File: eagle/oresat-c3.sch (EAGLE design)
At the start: 161 parts, among them J1 J-SAMTEC-TFM-110-X1-XXX-D-RA, J10 U.FL, J11 U.FL, J13 U.FL, J14 U.FL, J15 HARWIN-2X8X1.27, J19 HARWIN-2X8X1.27, J2 U.FL, J3 U.FL, J4 U.FL, J5 2-1734592-0, J6 J-SAMTEC-TFM-120-X1-XXX-D-RA, J8 U.FL, J9 U.FL, Q1 MOSFET-PCH-SOT23-6, U1 MAX892LEUA+T21-0036K-L, U11 U-ONSEMI-AX5043, U12 LP2985XX-N, U13 U-ONSEMI-AX5043, U14 LP2985XX-N, U2 TCAN330, U3 TCAN330, U4 TPS259621 - eFuse, U5 TPS62111RSA, U7 STM32F446RE, U8 UT01VS33DFLATDI_8, U9 SFEM016GB1EM1TO-A-HG-111-STD, X1 16MHZ-2.5x2mm, X3 TAITIEN-TY, X4 TAITIEN-TY

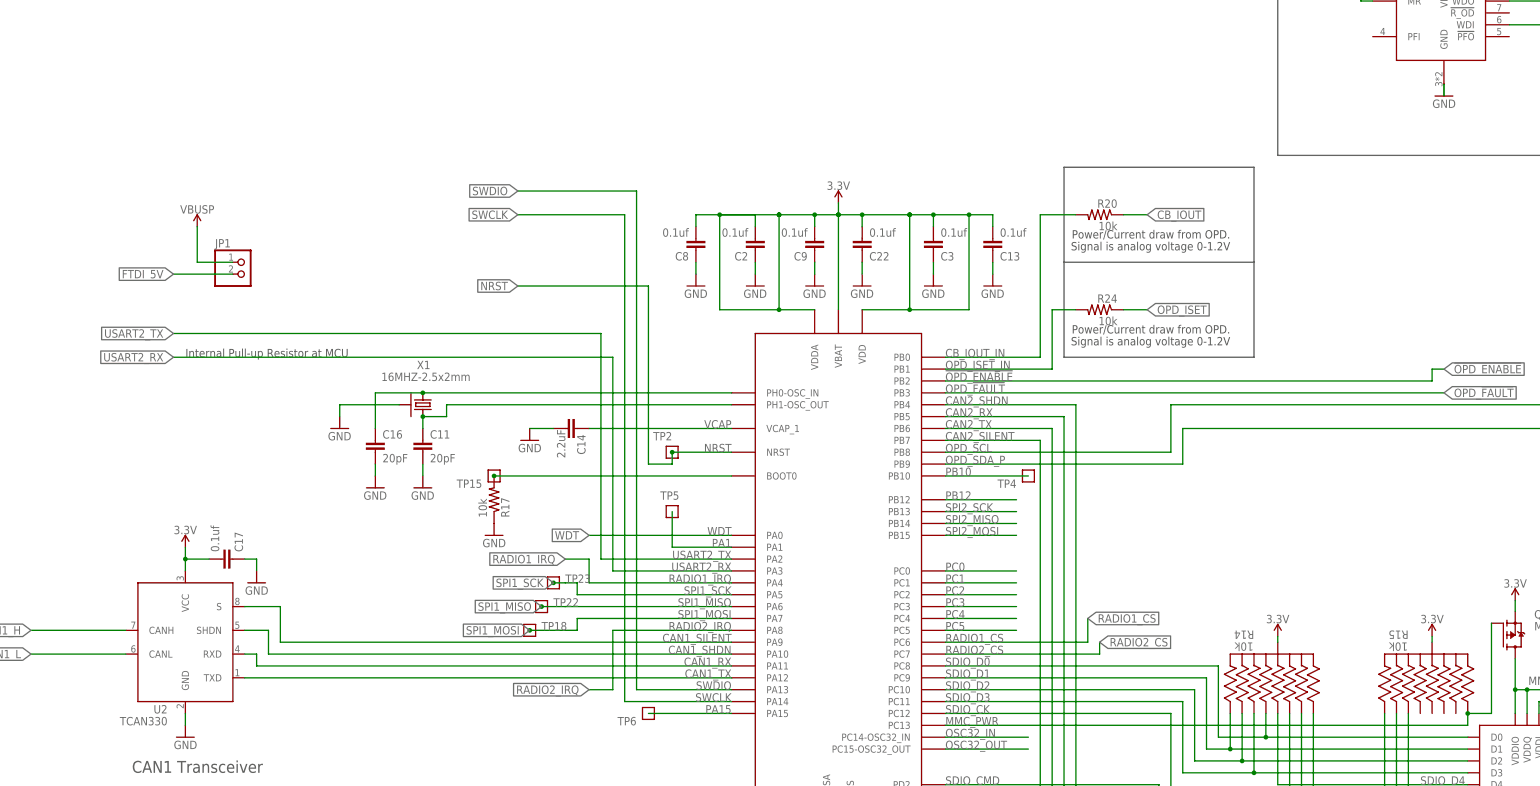
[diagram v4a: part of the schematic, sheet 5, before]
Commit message: Removed jumper Fixed DRC errors
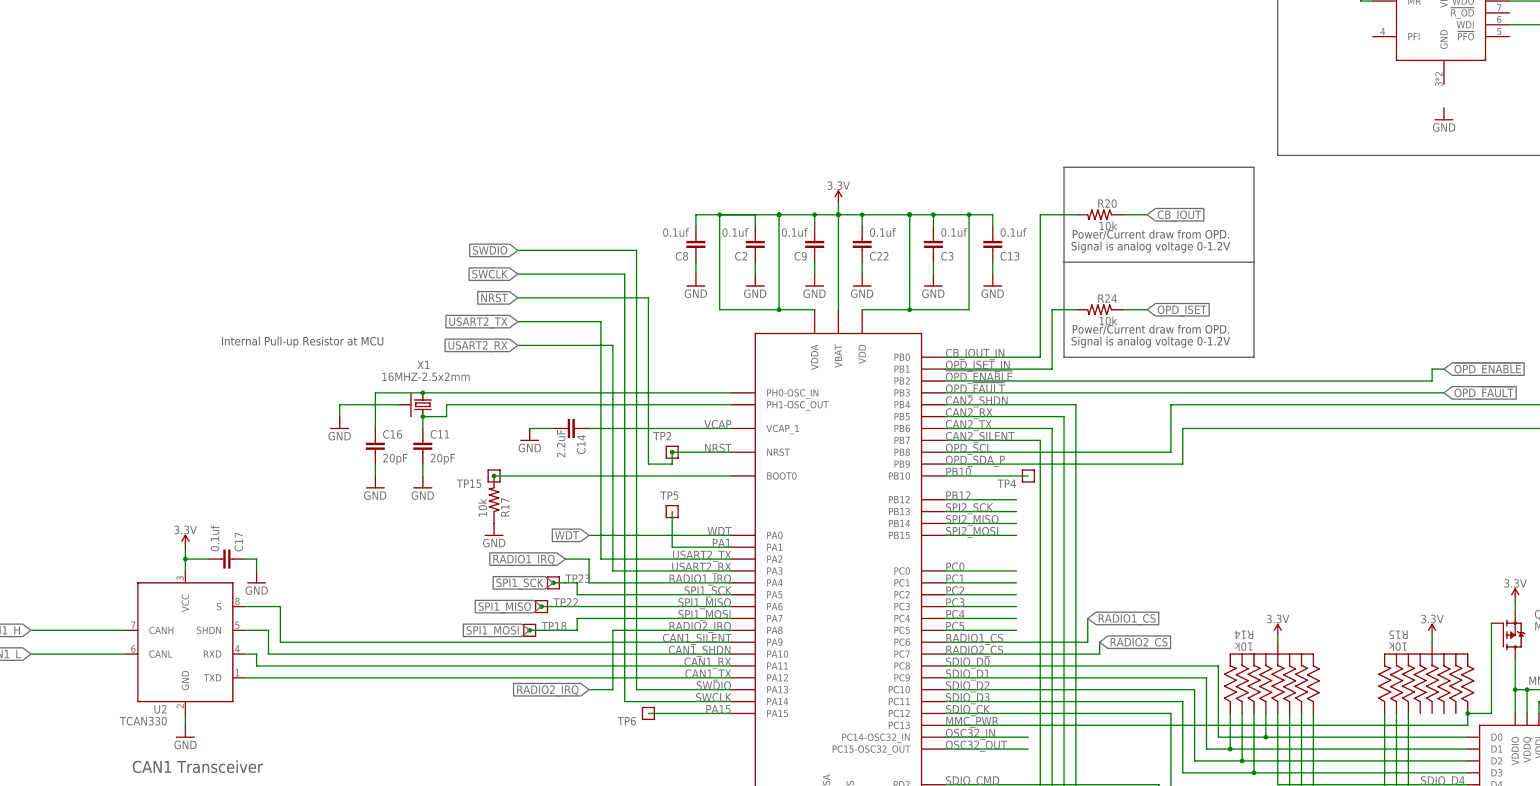
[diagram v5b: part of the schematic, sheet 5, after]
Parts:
- removed JP1: (no value), pinhead:PINHD-1X2
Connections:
- removed net FTDI_5V: J5.18, J5.19, JP1.2
- net GND: no longer U8.GND
- net VBUSP: now also J5.18, J5.19; no longer JP1.1
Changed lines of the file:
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@@
 <part name="GND59" library="supply1" library_urn="urn:adsk.eagle:library:371" deviceset="GND" device=""/>
 <part name="D6" library="D-LittelFuse-Uni-Directional-TVS" deviceset="SZ1SMB5.0AT3G" device="" package3d_urn="urn:adsk.eagle:package:17409861/1"/>
-<part name="JP1" library="pinhead" library_urn="urn:adsk.eagle:library:325" deviceset="PINHD-1X2" device="" package3d_urn="urn:adsk.eagle:package:22435/2"/>
-<part name="VBUSP3" library="oresat-supplies" deviceset="VBUSP" device=""/>
 <part name="U8" library="U-COBHAM-UT01VS33D-Voltage-Supervisor" deviceset="UT01VS33D" device="FLATDI_8" package3d_urn="urn:adsk.eagle:package:17466412/1"/>
 <part name="GND60" library="supply1" library_urn="urn:adsk.eagle:library:371" deviceset="GND" device=""/>
@@
 </segment>
 </net>
-<net name="FTDI_5V" class="0">
+<net name="VBUSP" class="0">
 <segment>
 <pinref part="J5" gate="G$1" pin="19"/>
@@
 <text x="332.74" y="264.16" size="3.81" layer="97">Watchdog</text>
 <wire x1="302.26" y1="180.34" x2="302.26" y2="160.02" width="0.1524" layer="97"/>
-<text x="73.66" y="160.02" size="1.778" layer="97">Internal Pull-up Resistor at MCU</text>
+<text x="81.28" y="162.56" size="1.778" layer="97">Internal Pull-up Resistor at MCU</text>
 <wire x1="302.26" y1="180.34" x2="261.62" y2="180.34" width="0.1524" layer="97"/>
 <wire x1="261.62" y1="180.34" x2="261.62" y2="200.66" width="0.1524" layer="97"/>
@@
 <attribute name="VALUE" x="73.66" y="66.294" size="1.778" layer="96" rot="MR0" align="bottom-center"/>
 </instance>
-<instance part="GND49" gate="1" x="342.9" y="215.9" smashed="yes" rot="MR0">
-<attribute name="VALUE" x="345.44" y="213.36" size="1.778" layer="96" rot="MR0"/>
+<instance part="GND49" gate="1" x="342.9" y="210.82" smashed="yes" rot="MR0">
+<attribute name="VALUE" x="345.44" y="208.28" size="1.778" layer="96" rot="MR0"/>
 </instance>
 <instance part="R8" gate="G$1" x="375.92" y="157.48" smashed="yes" rot="MR270">
@@
 <attribute name="VALUE" x="402.59" y="127" size="1.778" layer="96" rot="R270"/>
 </instance>
-<instance part="JP1" gate="G$1" x="86.36" y="177.8" smashed="yes">
-<attribute name="NAME" x="80.01" y="183.515" size="1.778" layer="95"/>
-<attribute name="VALUE" x="80.01" y="172.72" size="1.778" layer="96"/>
-</instance>
-<instance part="VBUSP3" gate="G$1" x="76.2" y="187.96" smashed="yes">
-<attribute name="VALUE" x="76.2" y="190.754" size="1.778" layer="96" align="bottom-center"/>
-</instance>
 <instance part="U8" gate="G$1" x="342.9" y="231.14" smashed="yes">
 <attribute name="NAME" x="330.5556" y="245.3386" size="2.0828" layer="95" ratio="6" rot="SR0"/>
@@
 </segment>
 <segment>
-<pinref part="GND49" gate="1" pin="GND"/>
-<wire x1="342.9" y1="215.9" x2="342.9" y2="218.44" width="0.1524" layer="91"/>
-<pinref part="U8" gate="G$1" pin="GND"/>
-</segment>
-<segment>
 <pinref part="C2" gate="G$1" pin="1"/>
 <pinref part="GND48" gate="1" pin="GND"/>
@@
 <segment>
 <wire x1="190.5" y1="116.84" x2="162.56" y2="116.84" width="0.1524" layer="91"/>
-<wire x1="162.56" y1="116.84" x2="162.56" y2="165.1" width="0.1524" layer="91"/>
+<wire x1="162.56" y1="116.84" x2="162.56" y2="167.64" width="0.1524" layer="91"/>
 <label x="190.5" y="116.84" size="1.778" layer="95" rot="MR0"/>
-<label x="71.12" y="165.1" size="1.778" layer="95" rot="R180" xref="yes"/>
+<label x="144.78" y="167.64" size="1.778" layer="95" rot="R180" xref="yes"/>
 <pinref part="U7" gate="G$1" pin="PA2"/>
-<wire x1="162.56" y1="165.1" x2="71.12" y2="165.1" width="0.1524" layer="91"/>
+<wire x1="162.56" y1="167.64" x2="144.78" y2="167.64" width="0.1524" layer="91"/>
 </segment>
 </net>
 <net name="USART2_RX" class="0">
 <segment>
-<wire x1="165.1" y1="114.3" x2="165.1" y2="160.02" width="0.1524" layer="91"/>
+<wire x1="165.1" y1="114.3" x2="165.1" y2="162.56" width="0.1524" layer="91"/>
 <wire x1="190.5" y1="114.3" x2="165.1" y2="114.3" width="0.1524" layer="91"/>
 <label x="190.5" y="114.3" size="1.778" layer="95" rot="MR0"/>
-<label x="71.12" y="160.02" size="1.778" layer="95" rot="R180" xref="yes"/>
+<label x="144.78" y="162.56" size="1.778" layer="95" rot="R180" xref="yes"/>
 <pinref part="U7" gate="G$1" pin="PA3"/>
-<wire x1="71.12" y1="160.02" x2="165.1" y2="160.02" width="0.1524" layer="91"/>
+<wire x1="144.78" y1="162.56" x2="165.1" y2="162.56" width="0.1524" layer="91"/>
 </segment>
 </net>
@@
 <net name="NRST" class="0">
 <segment>
-<wire x1="172.72" y1="137.16" x2="172.72" y2="175.26" width="0.1524" layer="91"/>
-<wire x1="172.72" y1="175.26" x2="144.78" y2="175.26" width="0.1524" layer="91"/>
+<wire x1="172.72" y1="137.16" x2="172.72" y2="172.72" width="0.1524" layer="91"/>
+<wire x1="172.72" y1="172.72" x2="144.78" y2="172.72" width="0.1524" layer="91"/>
 <pinref part="TP2" gate="G$1" pin="1"/>
 <pinref part="U7" gate="G$1" pin="NRST"/>
@@
 <junction x="177.8" y="139.7"/>
 <wire x1="177.8" y1="137.16" x2="172.72" y2="137.16" width="0.1524" layer="91"/>
-<label x="144.78" y="175.26" size="1.778" layer="95" rot="R180" xref="yes"/>
+<label x="144.78" y="172.72" size="1.778" layer="95" rot="R180" xref="yes"/>
 </segment>
 </net>
@@
 <wire x1="167.64" y1="86.36" x2="190.5" y2="86.36" width="0.1524" layer="91"/>
 <label x="190.5" y="86.36" size="1.778" layer="95" rot="MR0"/>
-<wire x1="167.64" y1="86.36" x2="167.64" y2="190.5" width="0.1524" layer="91"/>
-<wire x1="167.64" y1="190.5" x2="144.78" y2="190.5" width="0.1524" layer="91"/>
+<wire x1="167.64" y1="86.36" x2="167.64" y2="177.8" width="0.1524" layer="91"/>
+<wire x1="167.64" y1="177.8" x2="144.78" y2="177.8" width="0.1524" layer="91"/>
 <pinref part="U7" gate="G$1" pin="PA14"/>
-<label x="144.78" y="190.5" size="1.778" layer="95" rot="R180" xref="yes"/>
+<label x="144.78" y="177.8" size="1.778" layer="95" rot="R180" xref="yes"/>
 </segment>
 </net>
@@
 <wire x1="170.18" y1="88.9" x2="190.5" y2="88.9" width="0.1524" layer="91"/>
 <label x="190.5" y="88.9" size="1.778" layer="95" rot="MR0"/>
-<wire x1="170.18" y1="88.9" x2="170.18" y2="195.58" width="0.1524" layer="91"/>
-<wire x1="170.18" y1="195.58" x2="144.78" y2="195.58" width="0.1524" layer="91"/>
+<wire x1="170.18" y1="88.9" x2="170.18" y2="182.88" width="0.1524" layer="91"/>
+<wire x1="170.18" y1="182.88" x2="144.78" y2="182.88" width="0.1524" layer="91"/>
 <pinref part="U7" gate="G$1" pin="PA13"/>
-<label x="144.78" y="195.58" size="1.778" layer="95" rot="R180" xref="yes"/>
+<label x="144.78" y="182.88" size="1.778" layer="95" rot="R180" xref="yes"/>
 </segment>
 </net>
@@
 </segment>
 </net>
-<net name="VBUSP" class="0">
-<segment>
-<pinref part="JP1" gate="G$1" pin="1"/>
-<wire x1="83.82" y1="180.34" x2="76.2" y2="180.34" width="0.1524" layer="91"/>
-<wire x1="76.2" y1="180.34" x2="76.2" y2="187.96" width="0.1524" layer="91"/>
-<pinref part="VBUSP3" gate="G$1" pin="VBUSP"/>
-</segment>
-</net>
-<net name="FTDI_5V" class="0">
-<segment>
-<pinref part="JP1" gate="G$1" pin="2"/>
-<wire x1="83.82" y1="177.8" x2="71.12" y2="177.8" width="0.1524" layer="91"/>
-<label x="71.12" y="177.8" size="1.778" layer="95" rot="R180" xref="yes"/>
-</segment>
-</net>

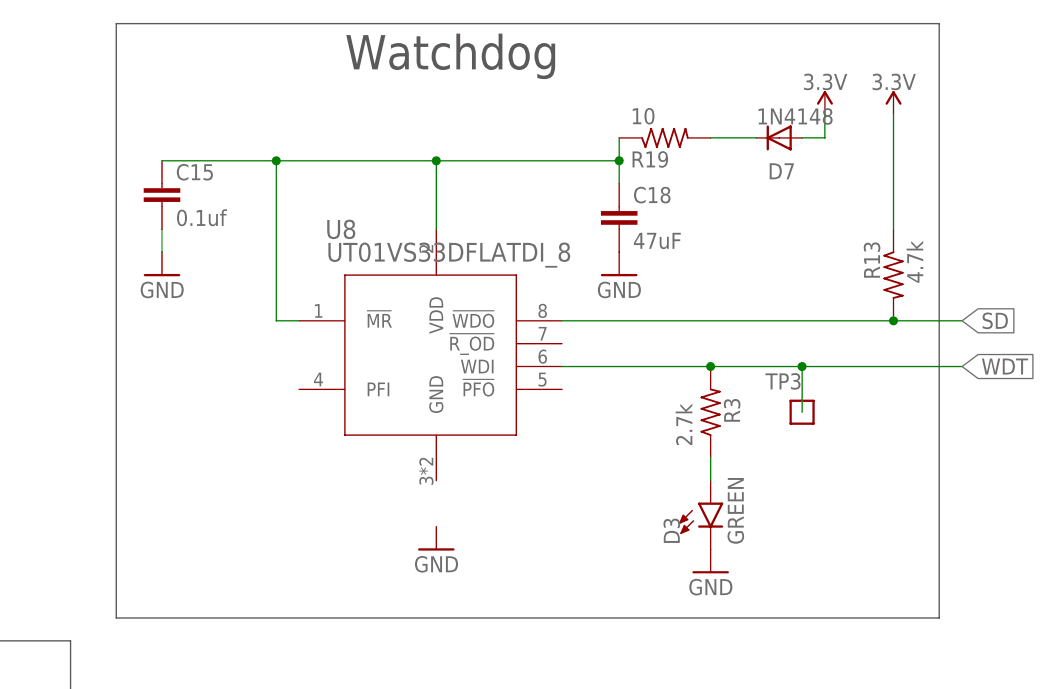
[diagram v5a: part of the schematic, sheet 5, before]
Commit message: Updated Eagle Brd/Schematic
Add Supervisory IC onto the C3 brd and schematic. Only implemented the watchdog timer functionality. The pins that are used to detect for brown out conditions have been left floating until further discussed.
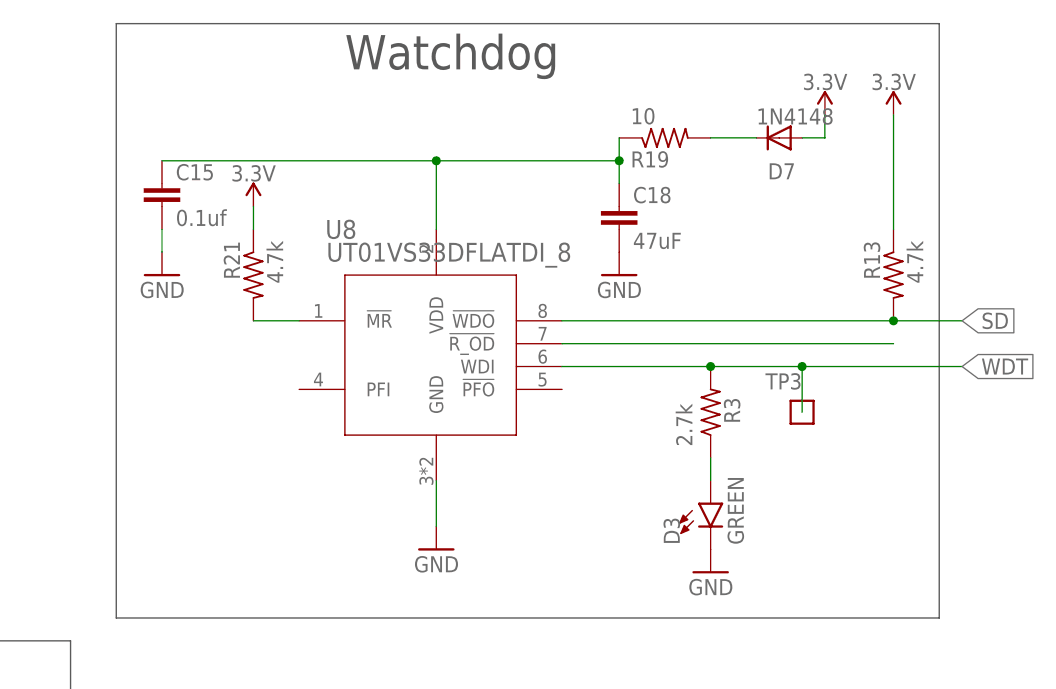
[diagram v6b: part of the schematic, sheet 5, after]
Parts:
- added R21: 4.7k, C3_SamacSys_Parts:R0603-4.7K-OHMS
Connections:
- new net N$4: R21.2, U8.!MR
- new net N$6: U8.!R_OD
- net 3.3V: now also R21.1
- net GND: now also U8.GND
- net WDT-PWR: no longer U8.!MR
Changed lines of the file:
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@@
 <part name="GND60" library="supply1" library_urn="urn:adsk.eagle:library:371" deviceset="GND" device=""/>
 <part name="GND61" library="supply1" library_urn="urn:adsk.eagle:library:371" deviceset="GND" device=""/>
+<part name="SUPPLY1" library="SparkFun-PowerSymbols" library_urn="urn:adsk.eagle:library:530" deviceset="3.3V" device=""/>
+<part name="R21" library="C3_SamacSys_Parts" deviceset="R0603-4.7K-OHMS" device="" value="4.7k"/>
 </parts>
 <sheets>
@@
 <attribute name="VALUE" x="330.6826" y="242.7986" size="2.0828" layer="96" ratio="6" rot="SR0"/>
 </instance>
+<instance part="SUPPLY1" gate="G$1" x="322.58" y="248.92" smashed="yes" rot="MR0">
+<attribute name="VALUE" x="322.58" y="251.714" size="1.778" layer="96" rot="MR0" align="bottom-center"/>
+</instance>
+<instance part="R21" gate="G$1" x="322.58" y="241.3" smashed="yes" rot="MR270">
+<attribute name="NAME" x="321.0814" y="245.11" size="1.778" layer="95" rot="MR270"/>
+<attribute name="VALUE" x="325.882" y="245.11" size="1.778" layer="96" rot="MR270"/>
+</instance>
 </instances>
 <busses>
@@
 <wire x1="396.24" y1="121.92" x2="396.24" y2="116.84" width="0.1524" layer="91"/>
 </segment>
+<segment>
+<pinref part="U8" gate="G$1" pin="GND"/>
+<pinref part="GND49" gate="1" pin="GND"/>
+<wire x1="342.9" y1="218.44" x2="342.9" y2="213.36" width="0.1524" layer="91"/>
+</segment>
 </net>
 <net name="CRYSTALIN" class="0">
@@
 <wire x1="358.14" y1="105.664" x2="358.14" y2="107.95" width="0.1524" layer="91"/>
 </segment>
+<segment>
+<pinref part="SUPPLY1" gate="G$1" pin="3.3V"/>
+<pinref part="R21" gate="G$1" pin="1"/>
+<wire x1="322.58" y1="248.92" x2="322.58" y2="246.38" width="0.1524" layer="91"/>
+</segment>
 </net>
 <net name="CAN1_RX" class="0">
@@
 <net name="WDT-PWR" class="0">
 <segment>
-<wire x1="327.66" y1="236.22" x2="325.12" y2="236.22" width="0.1524" layer="91"/>
-<wire x1="312.42" y1="254" x2="325.12" y2="254" width="0.1524" layer="91"/>
 <pinref part="C15" gate="G$1" pin="1"/>
-<wire x1="325.12" y1="236.22" x2="325.12" y2="254" width="0.1524" layer="91"/>
-<pinref part="U8" gate="G$1" pin="!MR"/>
 <pinref part="U8" gate="G$1" pin="VDD"/>
 <wire x1="342.9" y1="246.38" x2="342.9" y2="254" width="0.1524" layer="91"/>
-<wire x1="342.9" y1="254" x2="325.12" y2="254" width="0.1524" layer="91"/>
-<junction x="325.12" y="254"/>
+<wire x1="342.9" y1="254" x2="312.42" y2="254" width="0.1524" layer="91"/>
 <pinref part="R19" gate="G$1" pin="1"/>
 <pinref part="C18" gate="G$1" pin="1"/>
@@
 </segment>
 </net>
+<net name="N$6" class="0">
+<segment>
+<pinref part="U8" gate="G$1" pin="!R_OD"/>
+<wire x1="356.87" y1="233.68" x2="393.7" y2="233.68" width="0.1524" layer="91"/>
+</segment>
+</net>
+<net name="N$4" class="0">
+<segment>
+<pinref part="R21" gate="G$1" pin="2"/>
+<pinref part="U8" gate="G$1" pin="!MR"/>
+<wire x1="322.58" y1="236.22" x2="327.66" y2="236.22" width="0.1524" layer="91"/>
+</segment>
+</net>
